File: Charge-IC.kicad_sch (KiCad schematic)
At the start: 23 parts

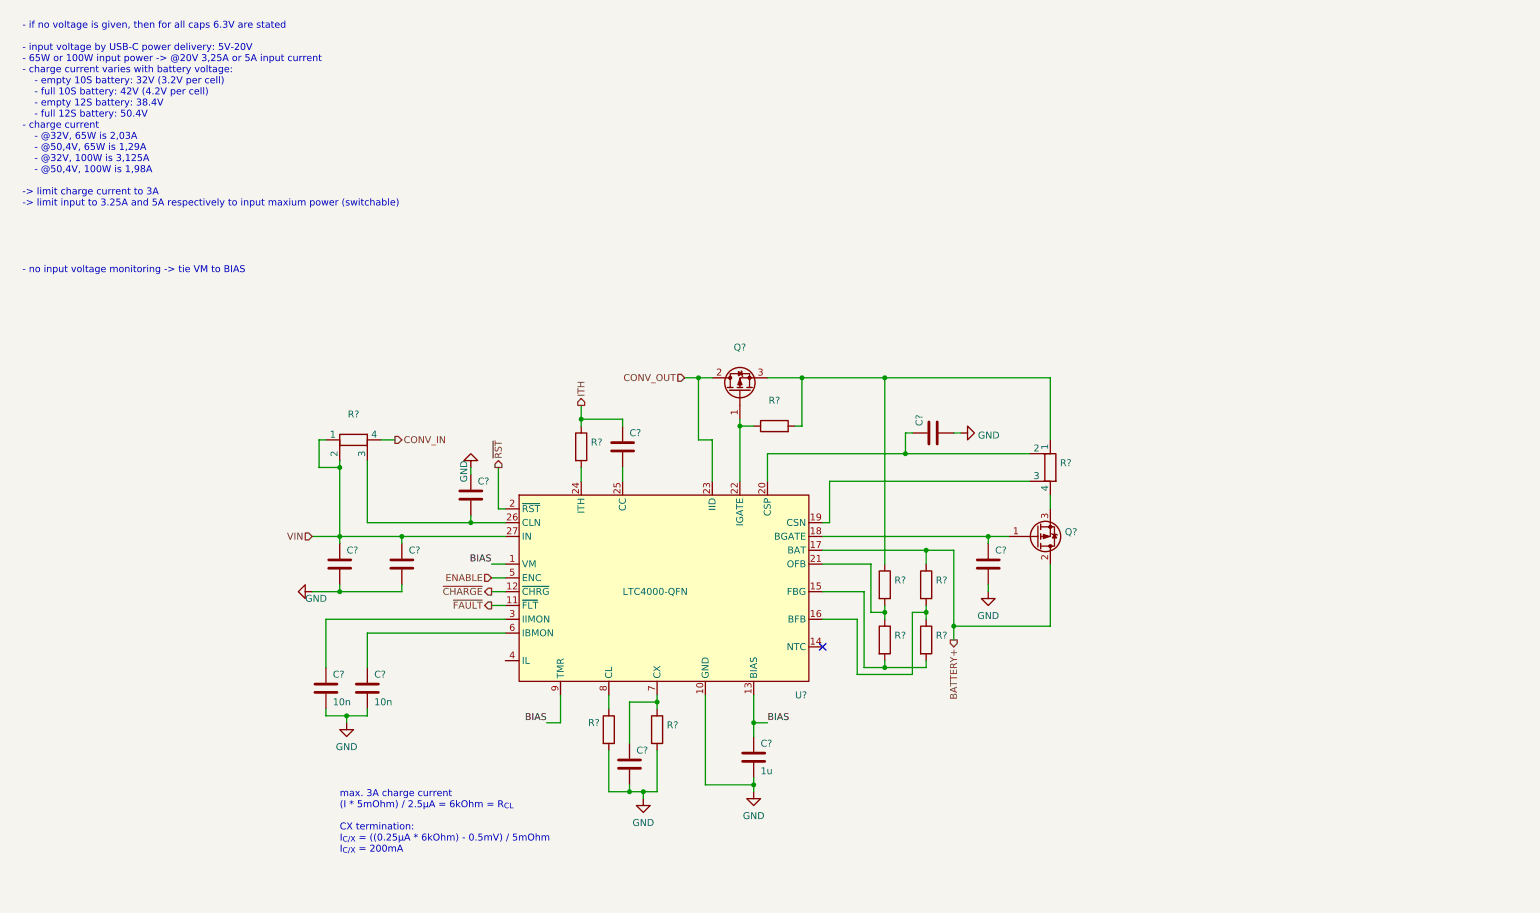
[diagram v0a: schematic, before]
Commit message: Finish Charge IC, WIP boost converter, add LTC3769
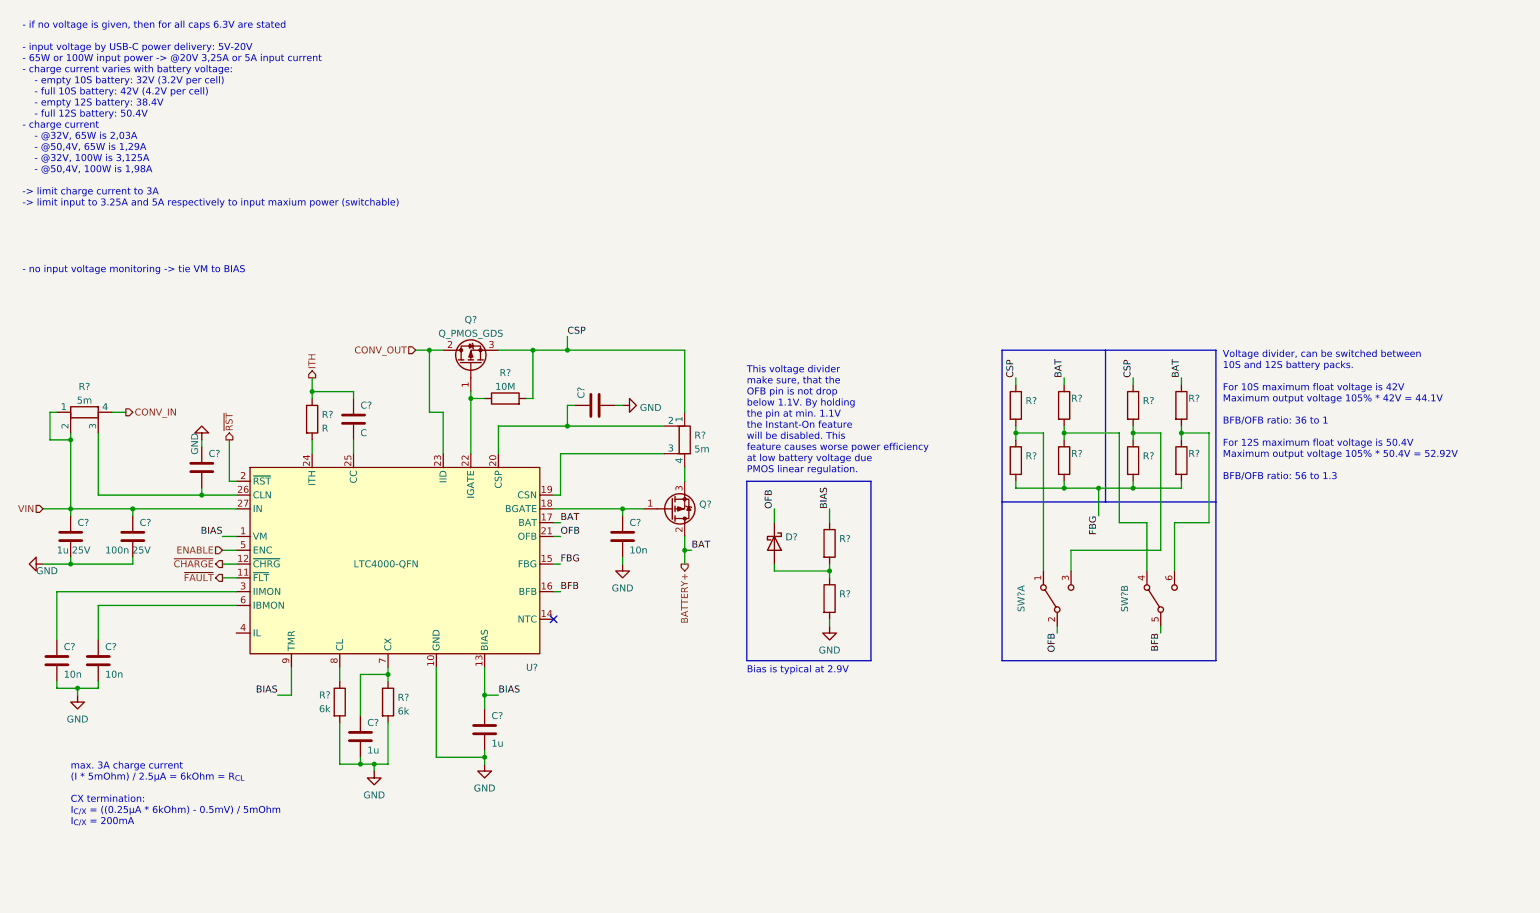
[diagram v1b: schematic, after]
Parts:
- added D?: (no value), symbol Device:D_Schottky
- added R? (x4): ~, symbol Device:R
- added R? (x2): (no value), symbol Device:R
- added SW? (x2): (no value), symbol Switch:SW_DPDT_x2
- C?: value (none) -> 1u
- C?: value (none) -> C
- C?: value (none) -> 10n
- C?: value (none) -> 100n 25V
- C?: value (none) -> 1u 25V
- Q?: value (none) -> Q_PMOS_GDS
- R? (x2): value (none) -> 6k
- R? (x3): value ~ -> (none)
- R?: value (none) -> 10M
- R? (x2): value (none) -> 5m
- R?: value (none) -> R
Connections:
- net BATTERY+: now also R?.1
- net BIAS: now also R?.1
- net GND: now also R?.2
- net FBG: now reaches R?.2, R?.2, U?.15 (FBG)
- net FBG: now also R?.2, R?.2
- net at R?.1, R?.2: now also SW?.4 (A); no longer U?.16 (BFB)
- net at R?.1, R?.2: now also SW?.1 (A); no longer U?.21 (OFB)
- net CSP: now reaches Q?.3 (S), R?.1, R?.1, R?.2
- net CSP: now also R?.1
- new net: R?.1, R?.2, SW?.3 (C)
- new net: D?.2 (A), R?.1, R?.2
- new net: R?.1, R?.2, SW?.6 (C)
- new net BFB: SW?.5 (B), U?.16 (BFB)
- new net OFB: D?.1 (K), SW?.2 (B), U?.21 (OFB)
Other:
- note added: "Bias is typical at 2.9V"
- note added: "This voltage divider make sure, that the OFB pin is not drop below 1.1V. By holding the pin at min. 1.1V the Instant-On feature will be disabled. This feature causes worse power efficiency at low battery voltage due PMOS linear regulation."
- note added: "Voltage divider, can be switched between 10S and 12S battery packs. For 10S maximum float voltage is 42V Maximum output voltage 105% * 42V = 44.1V BFB/OFB ratio: 36 to 1 For 12S maximum float voltage is 50.4V Maximum output voltage 105% * 50.4V = 52.92V BFB/OFB ratio: 56 to 1.3"
- moved on the sheet: C?, Q?, R?, U?

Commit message: WIP boost converter
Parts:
- added R?: 6k5, symbol Device:R
- added R?: 10k, symbol Device:R
- added SW?: SW_SPDT, symbol Switch:SW_SPDT
- C?: value 10n -> 10n 25V
- D?: value (none) -> D_Schottky
- R? (x2): value ~ -> 2M4
- R? (x2): value ~ -> 56k
- R?: value (none) -> 200k
- R? (x2): value (none) -> 3M3
- R? (x2): value (none) -> 91k
- R?: value (none) -> 330k
- SW? (x2): value (none) -> SW_DPDT_x2
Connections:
- net GND: now also R?.2, R?.2
- net at U?.4 (IL): now also SW?.2 (B)
- new net: R?.1, SW?.1 (A)
- new net: R?.1, SW?.3 (C)
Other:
- note added: "input current limit: R = (I_{ILIM} * 5mOhm) / 2.5µA R_{@3.25A} = 6.5kOhm R_{@5A} = 10kOhm"

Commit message: Finish boost converter
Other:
- note added: "- input voltage by USB-C power delivery: 5V-20V - 65W or 100W input power -> @20V 3,25A or 5A input current - charge current varies with battery voltage: - empty 10S battery: 32V (3.2V per cell) - full 10S battery: 42V (4.2V per cell) - empty 12S battery: 38.4V - full 12S battery: 50.4V - charge current - @32V, 65W is 2,03A - @50,4V, 65W is 1,29A - @32V, 100W is 3,125A - @50,4V, 100W is 1,98A -> 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"
- note removed: "- if no voltage is given, then for all caps 6.3V are stated - input voltage by USB-C power delivery: 5V-20V - 65W or 100W input power -> @20V 3,25A or 5A input current - charge current varies with battery voltage: - empty 10S battery: 32V (3.2V per cell) - full 10S battery: 42V (4.2V per cell) - empty 12S battery: 38.4V - full 12S battery: 50.4V - charge current - @32V, 65W is 2,03A - @50,4V, 65W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"
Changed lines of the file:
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@@
     (effects (font (size 1.27 1.27)) (justify left bottom))
   )
-  (text "- if no voltage is given, then for all caps 6.3V are stated\n\n- input voltage by USB-C power delivery: 5V-20V\n- 65W or 100W input power -> @20V 3,25A or 5A input current\n- charge current varies with battery voltage:\n	- empty 10S battery: 32V (3.2V per cell)\n	- full 10S battery: 42V (4.2V per cell)\n	- empty 12S battery: 38.4V\n	- full 12S battery: 50.4V\n- charge current \n	- @32V, 65W is 2,03A\n	- @50,4V, 65W is 1,29A\n	- @32V, 100W is 3,125A\n	- @50,4V, 100W is 1,98A\n\n-> limit charge current to 3A\n-> limit input to 3.25A and 5A respectively to input maxium power (switchable)\n\n- no input voltage monitoring -> tie VM to BIAS\n- no timeout -> TMR to BIAS"
-    (at 13.97 55.88 0)
+  (text "- input voltage by USB-C power delivery: 5V-20V\n- 65W or 100W input power -> @20V 3,25A or 5A input current\n- charge current varies with battery voltage:\n	- empty 10S battery: 32V (3.2V per cell)\n	- full 10S battery: 42V (4.2V per cell)\n	- empty 12S battery: 38.4V\n	- full 12S battery: 50.4V\n- charge current \n	- @32V, 65W is 2,03A\n	- @50,4V, 65W is 1,29A\n	- @32V, 100W is 3,125A\n	- @50,4V, 100W is 1,98A\n\n-> limit charge current to 3A\n-> limit input to 3.25A and 5A respectively to input maxium power (switchable)\n\n- no input voltage monitoring -> tie VM to BIAS\n- no timeout -> TMR to BIAS"
+    (at 13.97 50.8 0)
     (effects (font (size 1.27 1.27)) (justify left bottom))
   )

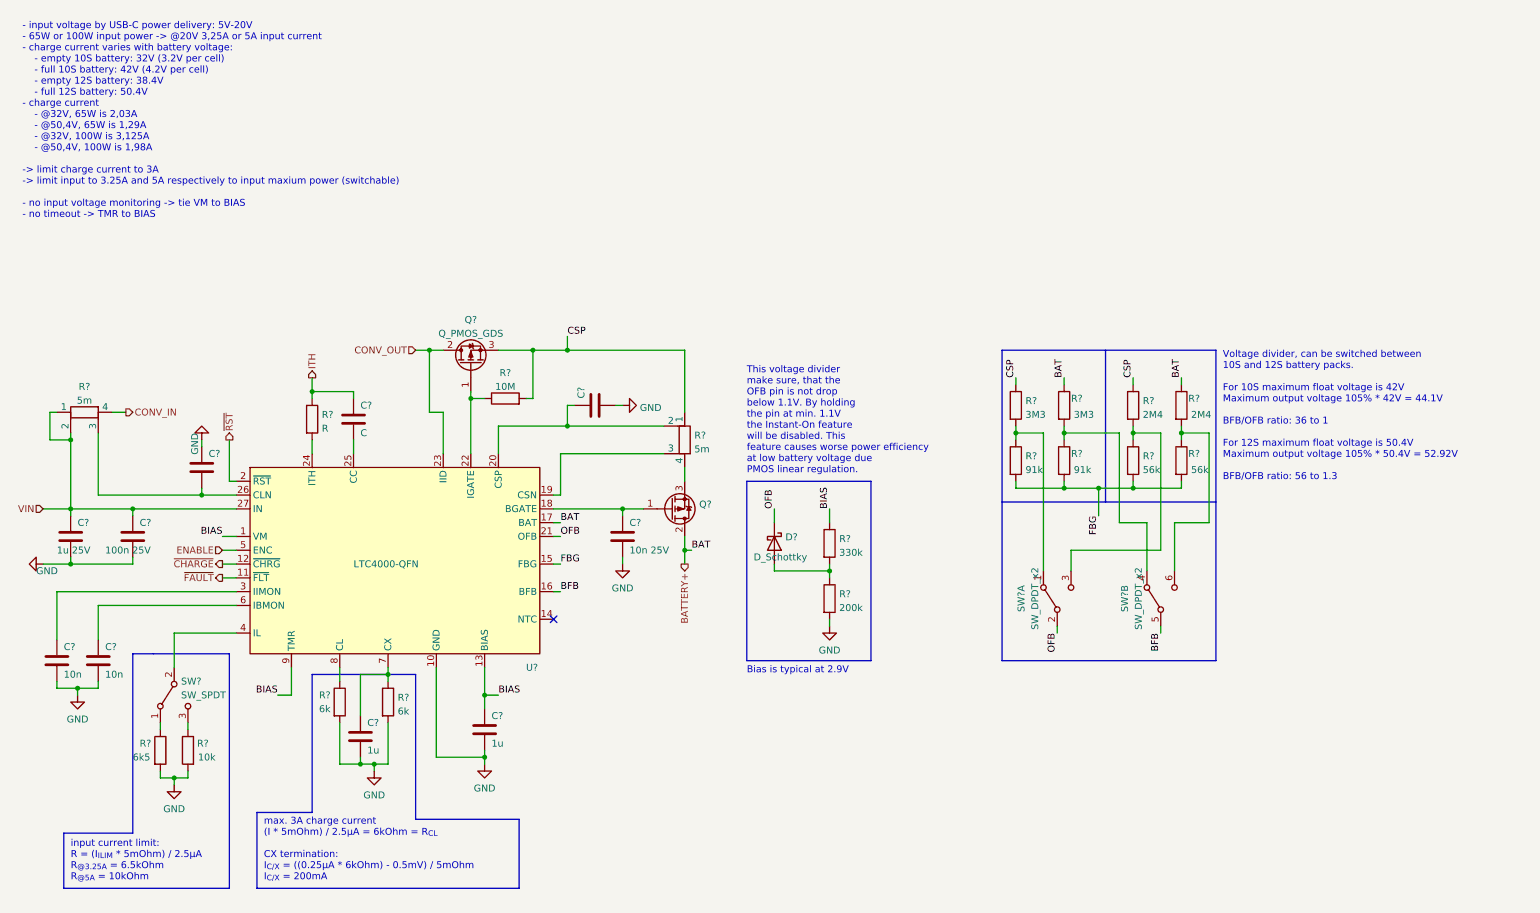
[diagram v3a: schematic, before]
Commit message: Finish schematic
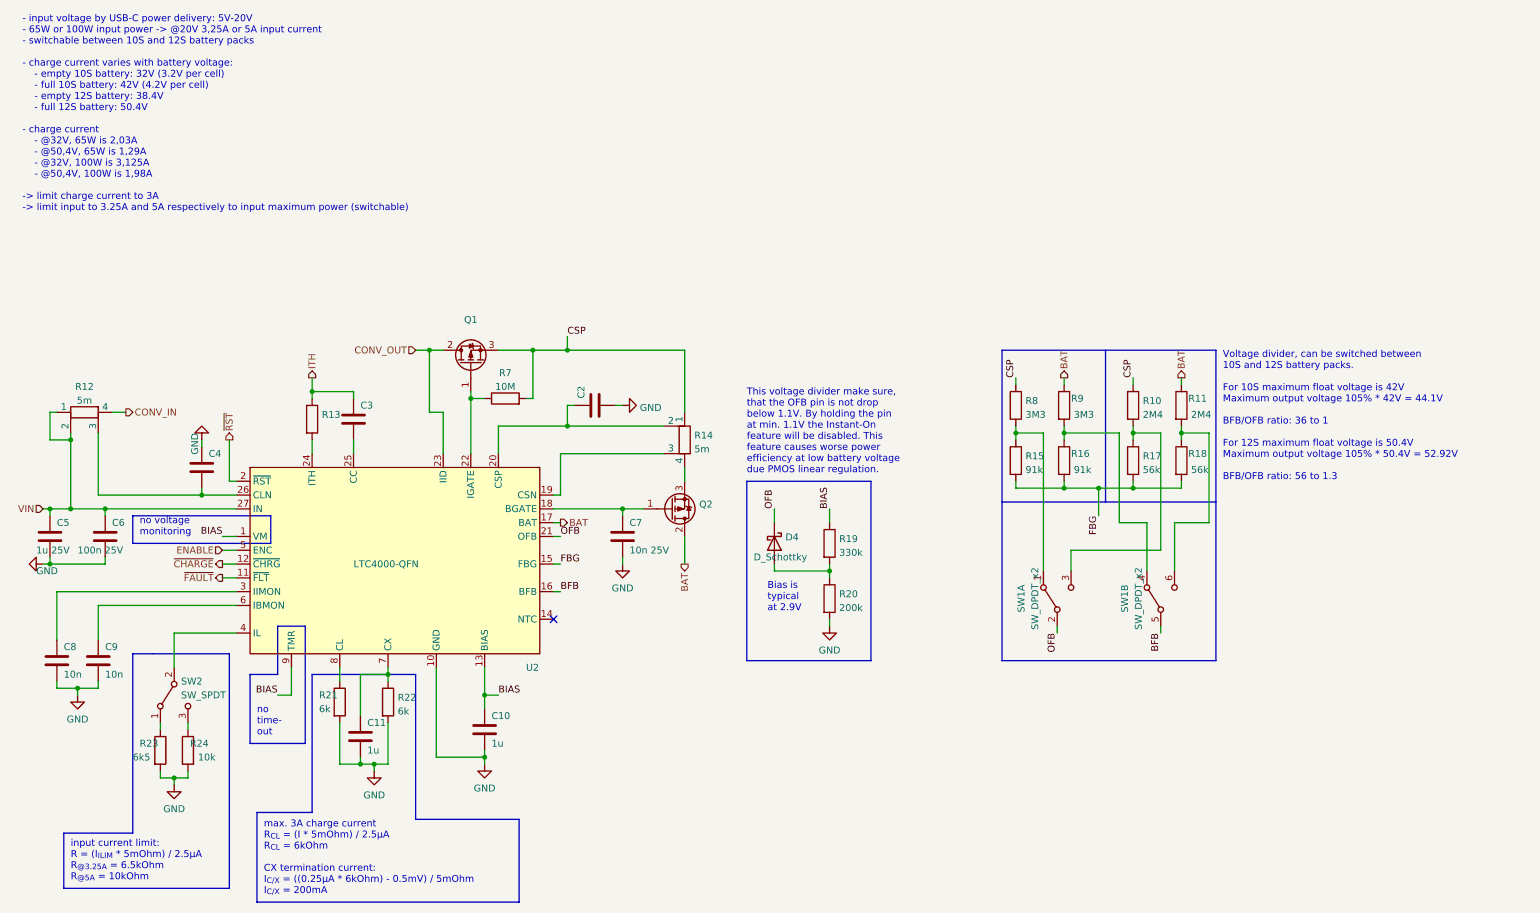
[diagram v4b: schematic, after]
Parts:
- C3: renamed from C?; value C -> (none)
- Q1: renamed from Q?; value Q_PMOS_GDS -> (none)
- Q2: renamed from Q?; value ~ -> (none)
- R13: renamed from R?; value R -> (none)
- gave numbers to parts that had none: 30
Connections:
- net BATTERY+ renamed BAT
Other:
- note added: "- input voltage by USB-C power delivery: 5V-20V - 65W or 100W input power -> @20V 3,25A or 5A input current - switchable between 10S and 12S battery packs - charge current varies with battery voltage: - empty 10S battery: 32V (3.2V per cell) - full 10S battery: 42V (4.2V per cell) - empty 12S battery: 38.4V - full 12S battery: 50.4V - charge current - @32V, 65W is 2,03A - @50,4V, 65W is 1,29A - @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"
- note added: "max. 3A charge current R_{CL} = (I * 5mOhm) / 2.5µA R_{CL} = 6kOhm CX termination current: I_{C/X} = ((0.25µA * 6kOhm) - 0.5mV) / 5mOhm I_{C/X} = 200mA"
- note added: "no time- out"
- note added: "no voltage monitoring"
- note removed: "- input voltage by USB-C power delivery: 5V-20V - 65W or 100W input power -> @20V 3,25A or 5A input current - charge current varies with battery voltage: - empty 10S battery: 32V (3.2V per cell) - full 10S battery: 42V (4.2V per cell) - empty 12S battery: 38.4V - full 12S battery: 50.4V - charge current - @32V, 65W is 2,03A - @50,4V, 65W is 1,29A - @32V, 100W is 3,125A - @50,4V, 100W is 1,98A -> 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"
- note removed: "max. 3A charge current (I * 5mOhm) / 2.5µA = 6kOhm = R_{CL} CX termination: I_{C/X} = ((0.25µA * 6kOhm) - 0.5mV) / 5mOhm I_{C/X} = 200mA"
- moved on the sheet: C5, C6

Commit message: Small changes
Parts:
- C10, C11, C5, C6, C7, C8, C9: footprint (none) -> Capacitor_SMD:C_0603_1608Metric
- C2: value ~ -> (none); footprint (none) -> Capacitor_SMD:C_0603_1608Metric
- C3: value (none) -> 47n; footprint (none) -> Capacitor_SMD:C_0603_1608Metric
- C4: value ~ -> (none)
- Q1, Q2: value (none) -> PMOS
- R10, R11, R15, R16, R17, R18, R19, R20, R21, R22, R23, R24, R7, R8, R9: footprint (none) -> Resistor_SMD:R_0603_1608Metric
- R13: value (none) -> 22k; footprint (none) -> Resistor_SMD:R_0603_1608Metric
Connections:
- net ITH: now also U2.24 (ITH); no longer C3.1
- net at R13.2: now also C3.1; no longer U2.24 (ITH)
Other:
- moved on the sheet: R13

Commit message: Annotate symbols and assign footprints
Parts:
- C10, C11: value 1u -> 1uF
- C2: value (none) -> DNP
- C3: value 47n -> 47nF
- C4: value (none) -> DNP; footprint (none) -> Capacitor_SMD:C_0603_1608Metric
- C5: value 1u 25V -> 1uF 25V
- C6: value 100n 25V -> 100nF 25V
- C7: value 10n 25V -> 10nF 25V
- C8, C9: value 10n -> 10nF
- D4: value D_Schottky -> CFSH05-20L; footprint (none) -> extraFootprints:SOD882D
- Q1, Q2: value PMOS -> RSJ250P10; footprint (none) -> Package_TO_SOT_SMD:TO-263-2
- R13: renamed from R12; footprint (none) -> extraFootprints:R_1206_3216Metric_4Kelvin
- R14: footprint (none) -> extraFootprints:R_1206_3216Metric_4Kelvin
- SW1: footprint (none) -> extraFootprints:SW_E-Switch_EG2201_DPDT
- SW2: footprint (none) -> extraFootprints:SW_E-Switch_EG1249_SPDT
- renumbered R9 to R10, R10 to R11, R11 to R12, R13 to R7, R7 to R8, R8 to R9
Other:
- note added: "this controls the DC/DC converter"
- moved on the sheet: R7
